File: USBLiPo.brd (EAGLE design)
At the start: 26.7 x 15.2 mm, 15 parts, among them IC1 LTC4054, Q1 2N7002, X1 USBSF-MICROB

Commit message: Final changes for v1.0 release
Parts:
- removed B1: 2P-JST-PTH, freetronics-jon:FREETRONICS-LUKE_JST-2MM-TH-RA
- removed X1: USBSF-MICROB, freetronics-jon:USB-MICROB
- added SJ1, SJ2: SJ, freetronics-luke:SJ
- C1: value 1uF -> 1uF 0603
- F1: value 500mA PTC -> 500mA PTC 1812
- LED1: value Charge -> ORANGE 0603
- LED2: value Standby -> GREEN 0603
- Q1: value 2N7002 -> 2N7002 SOT-23
- R1, R4, R5: value 10K -> 10K 0603
- R2: value 1K -> 1K 0603
- R3: value 3K3 -> 3K3 0603
- S1: value SJ -> USBSF-MICROB; device freetronics-luke:SJ -> freetronics-jon:USB-MICROB
- S2: value SJ -> 2P-JST-PTH; device freetronics-luke:SJ -> freetronics-jon:FREETRONICS-LUKE_JST-2MM-TH-RA
- moved S1 20.7 mm to (1.40, 7.62), turned to 270 degrees
- moved S2 4.77 mm to (24.1, 7.62), turned to 270 degrees
- moved R3 0.39 mm to (19.3, 2.79)
- moved R4 0.25 mm to (16.6, 1.11)
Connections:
- net GND: now also S1.FIX1, S1.FIX2, S1.GND, S1.TAB1, S1.TAB2, S2.NEG; no longer B1.NEG, X1.FIX1, X1.FIX2, X1.GND, X1.TAB1, X1.TAB2
- net N$113: now also S1.VBUS; no longer X1.VBUS
- net N$3: now also SJ1.2, SJ2.2; no longer S1.2, S2.2
- net N$4: now also S2.POS; no longer B1.POS
- net N$5: now also SJ1.1; no longer S1.1
- net N$7: now also SJ2.1; no longer S2.1
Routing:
- net GND: track 5.92 -> 1.32 mm, vias 18 -> 15
- net N$6: track 15.9 -> 14.7 mm
- net N$3: track 22.6 -> 23.2 mm
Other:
- board text added: "1 0 300 mA"
- board text added: "1 1 500 mA"
- board text added: "100-500mA"
- board text added: "1= closed"
- board text added: "LiPo CHARGER"
- board text added: "SJ1"
- board text added: "SJ1 SJ2 Charge Current"
- board text added: "SJ2"
- board text added: "USB LiPo Single Cell Charger"
- board text added: "V1.0 SKU: USBLIPO"
- board text removed: "1 0 303 mA"
- board text removed: "1 1 503 mA"
- board text removed: "1= short"
- board text removed: "LiPo charger"
- board text removed: "S1"
- board text removed: "S1 S2 Charge Current"
- board text removed: "S2"
- board text removed: "SKU: USBLIPO"
- board text removed: "USB LiPo cell charger"

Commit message: Changed USB socket to strong footprint; added 0.1 battery connector
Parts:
- removed S1: USBSF-MICROB, freetronics-jon:USB-MICROB
- added H1: USB-6PSMT, freetronics-jon:USB-MICROB-MB05PMXX
- added H3: (no value), freetronics-master-v1.1:1X02
- renumbered S2 to H2
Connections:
- net GND: now also H1.FIX1, H1.FIX2, H1.GND, H1.PIN1, H1.PIN2, H1.TAB1, H1.TAB2, H3.2; no longer S1.FIX1, S1.FIX2, S1.GND, S1.TAB1, S1.TAB2
- net N$113: now also H1.VBUS; no longer S1.VBUS
- net N$4: now also H3.1
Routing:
- net GND: track 1.32 -> 6.18 mm, vias 15 -> 11
- net N$3: track 23.2 -> 21.7 mm
- net N$113: track 5.75 -> 4.88 mm
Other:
- board text added: "SJ1 SJ2 Charge Rate"
- board text added: "V1.1 SKU: USBLIPO"
- board text removed: "SJ1 SJ2 Charge Current"
- board text removed: "V1.0 SKU: USBLIPO"

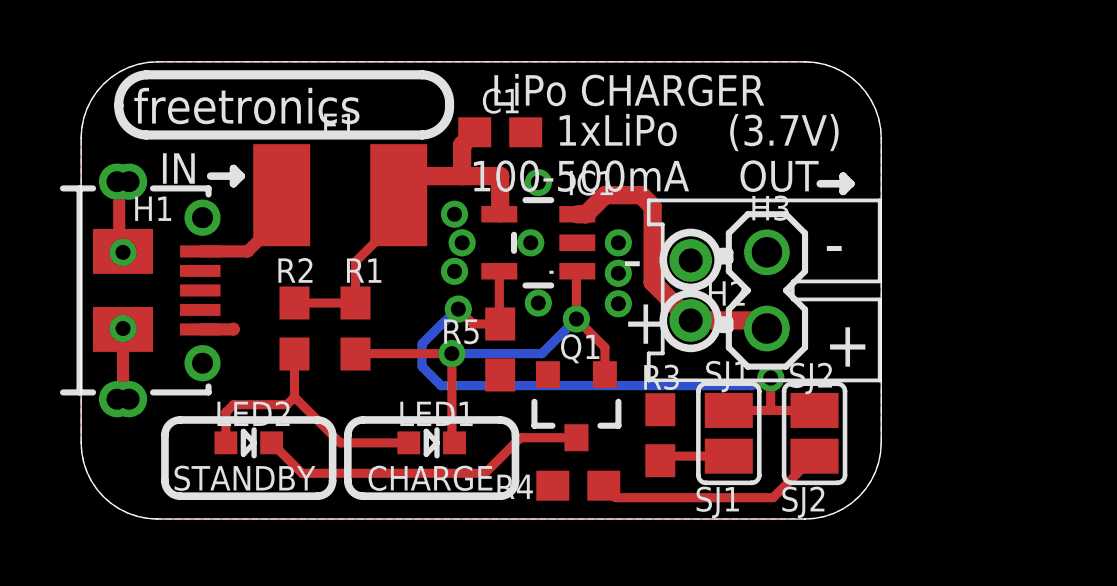
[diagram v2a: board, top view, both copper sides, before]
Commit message: Switched pads to bottom; shorter board; ready for v1.1 release
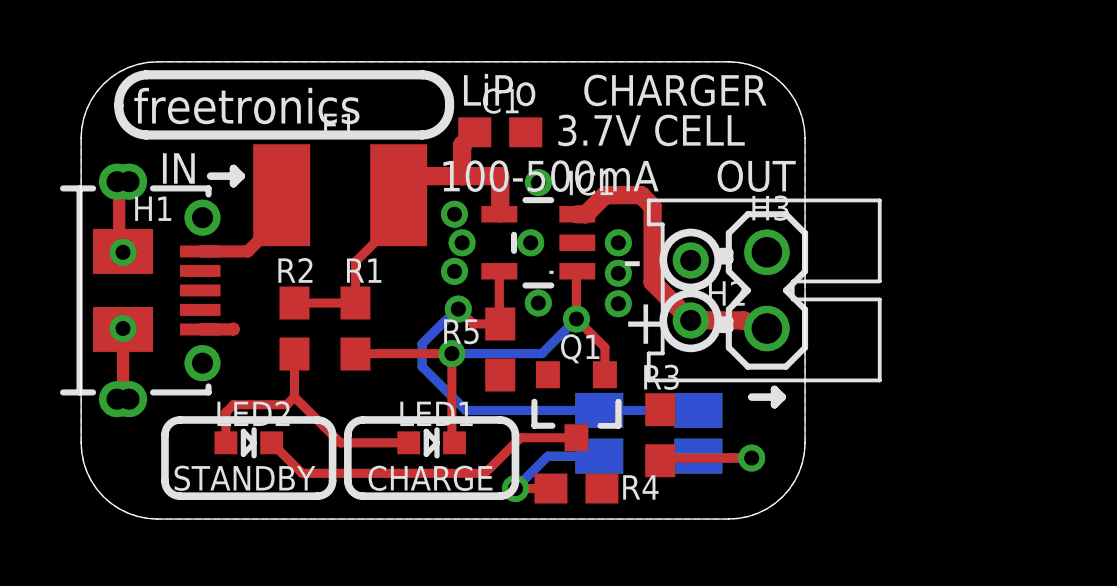
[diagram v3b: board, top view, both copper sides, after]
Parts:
- H2: device freetronics-jon:FREETRONICS-LUKE_JST-2MM-TH-RA -> freetronics-jon:JST-2MM-TH-RA
- moved SJ2 7.18 mm to (17.3, 2.86), flipped to the bottom
- moved SJ1 1.02 mm to (20.6, 2.86), flipped to the bottom
- moved R4 0.11 mm to (16.5, 1.02), turned to 0 degrees
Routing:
- net N$3: track 21.7 -> 15.6 mm, vias 2 -> 1
- net N$7: track 7.76 -> 4.42 mm, vias 0 -> 1
- net N$5: track 2.33 -> 4.89 mm, vias 0 -> 1
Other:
- board size 26.7 x 15.2 mm -> 24.1 x 15.2 mm
- board text added: "3.7V CELL"
- board text added: "CHARGER"
- board text added: "Cell Charger"
- board text added: "LiPo"
- board text added: "SKU: USBLIPO"
- board text added: "USB LiPo Single"
- board text added: "V1.1"
- board text removed: "(3.7V)"
- board text removed: "0= open"
- board text removed: "1= closed"
- board text removed: "1xLiPo"
- board text removed: "LiPo CHARGER"
- board text removed: "USB LiPo Single Cell Charger"
- board text removed: "V1.1 SKU: USBLIPO"

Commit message: Fix silkscreen error, one charge current setting was wrong Bump version to 1.2.
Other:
- board text added: "1 0 400 mA"
- board text added: "V1.2"
- board text removed: "1 0 300 mA"
- board text removed: "V1.1"
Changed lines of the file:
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@@
 <?xml version="1.0" encoding="utf-8"?>
 <!DOCTYPE eagle SYSTEM "eagle.dtd">
-<eagle version="6.3">
+<eagle version="6.5.0">
 <drawing>
 <settings>
@@
 <layer number="19" name="Unrouted" color="12" fill="1" visible="yes" active="yes"/>
 <layer number="20" name="Dimension" color="15" fill="1" visible="yes" active="yes"/>
-<layer number="21" name="tPlace" color="15" fill="1" visible="yes" active="yes"/>
+<layer number="21" name="tPlace" color="15" fill="1" visible="no" active="yes"/>
 <layer number="22" name="bPlace" color="14" fill="1" visible="yes" active="yes"/>
 <layer number="23" name="tOrigins" color="15" fill="1" visible="yes" active="yes"/>
@@
 <text x="19.558" y="12.827" size="1.016" layer="22" ratio="15" rot="MR0">0   0   100 mA</text>
 <text x="19.558" y="11.6205" size="1.016" layer="22" ratio="15" rot="MR0">0   1   200 mA</text>
-<text x="19.558" y="10.414" size="1.016" layer="22" ratio="15" rot="MR0">1   0   300 mA</text>
+<text x="19.558" y="10.414" size="1.016" layer="22" ratio="15" rot="MR0">1   0   400 mA</text>
 <text x="19.558" y="9.2075" size="1.016" layer="22" ratio="15" rot="MR0">1   1   500 mA</text>
 <wire x1="3.302" y1="3.302" x2="7.874" y2="3.302" width="0.254" layer="21"/>
@@
 <wire x1="21.59" y1="6.604" x2="21.59" y2="6.35" width="0.3048" layer="21"/>
 <wire x1="21.59" y1="6.35" x2="21.336" y2="6.35" width="0.3048" layer="21"/>
-<text x="3.683" y="12.2555" size="1.016" layer="22" font="vector" ratio="17" rot="SMR0">V1.1</text>
+<text x="3.683" y="12.2555" size="1.016" layer="22" font="vector" ratio="17" rot="SMR0">V1.2</text>
 <text x="15.494" y="2.032" size="1.016" layer="22" font="vector" ratio="17" rot="SMR0">Cell Charger</text>
 <text x="16.7005" y="13.7795" size="1.016" layer="21" ratio="15">CHARGER</text>
